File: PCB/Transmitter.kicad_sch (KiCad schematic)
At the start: 31 parts, among them T1 MABA-007159, U1 LTC5599IUF, U2 ADF4351

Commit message: new file:   Datasheet/HMC849A_RF_Switch_SPDT.pdf 	new file:   Datasheet/TG2016SMN_26MHz_MCGNNM_Oscillator.pdf 	modified:   PCB/DroidRadio.kicad_pro 	modified:   PCB/DroidRadio.kicad_sch 	modified:   PCB/Processors.kicad_sch 	modified:   PCB/Simulation/Transmitter_Side.pll 	modified:   PCB/Transmitter.kicad_sch 	deleted:    PCB/~DroidRadio.kicad_pro.lck
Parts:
- added C10, C23, C25: 10pF, symbol Device:C
- added C22, C24, C26, C28, C29, C30, C31, C32, C33, C34, C35, C9: 0.1uF, symbol Device:C
- added C27: 2.2nF, symbol Device:C
- added FL1: LFCN-1400, Filter:Filter_Mini-Circuits_FV1206, symbol RF_Filter:LFCN-1400
- added FL2: LFCN-2000, Filter:Filter_Mini-Circuits_FV1206, symbol RF_Filter:LFCN-2000
- added R7: 25.1k, symbol Device:R_US
- added R8: 23.1k, symbol Device:R_US
- added U3, U4: HMC849A, Package_DFN_QFN:QFN-24-1EP_4x4mm_P0.5mm_EP2.65x2.65mm_ThermalVias, symbol RF_Switch:HMC849A
- added Y1: TG2016SMN-26Mhz-MCGNNM, Crystal:Crystal_SMD_2016-4Pin_2.0x1.6mm, symbol Oscillator:TG2520SMN-xx.xxxxxxMhz-xxxxNM
- C17: value 2.7nF -> 3nF; Tolerance (none) -> 1%
- C18: value 220uF -> 30pF; Tolerance (none) -> 1%
- C19: value 0.1uF -> 39nF; Tolerance (none) -> 1%
- C20: value 1nF -> 1.2nF; Tolerance (none) -> 1%
- C21: value 330pF -> 180pF; Tolerance (none) -> 1%
- R2: value 5.1k, 1% -> 5.1k; Tolerance (none) -> 1%
- R3: value 220 -> 216; Tolerance (none) -> 1%
- R4: value 5 -> 19.1k
- R5: value 430 -> 442; Tolerance (none) -> 1%
- R6: value 30 -> 26.1k
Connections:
- net +3.3V: now also C9.2, Y1.4 (Vcc)
- net GND: now also C10.1, C22.1, C23.1, C24.1, C25.1, C26.1, C27.2, C28.1, C29.2, C9.1, FL1.2 (GND), FL1.4 (GND), FL2.2 (GND), FL2.4 (GND), U3.10 (GND), U3.11 (GND), U3.13 (GND), U3.14 (GND), U3.15 (GND), U3.16 (GND), U3.17 (GND), U3.4 (GND), U3.6 (GND), U3.7 (GND), U3.8 (GND), U4.10 (GND), U4.11 (GND), U4.13 (GND), U4.14 (GND), U4.15 (GND), U4.16 (GND), U4.17 (GND), U4.4 (GND), U4.6 (GND), U4.7 (GND), U4.8 (GND), Y1.2 (GND)
- net SPI_CLK: now also R7.2
- net at C1.1, L1.1: no longer T1.5
- net at C19.1: now also R3.2, C27.1; no longer R4.2
- net at C20.1, C21.1, U2.20 (VTUNE): now also R5.2; no longer R6.2
- net at C5.2, U1.19 (CSB): now also R8.1
- net at R6.1: now also C3.2, U1.21 (SDI); no longer R5.2
- net at C4.2, U1.20 (SCLK): now also R7.1
- net at R2.1: now also U2.22 (RSET); no longer U2.24 (VREF)
- net at R4.1: now also C2.2, R1.2, U1.22 (SDO); no longer R3.2
- net TXRF: now reaches U1.16 (RF)
- net SYN_RF_1P: now reaches U2.14 (RF_OUT_B+)
- net SYN_RF_1P: now also U2.15 (RF_OUT_B-)
- net at U2.19 (TEMP): now also C10.2, C22.2
- net at U2.23 (VCOM): now also C23.2, C24.2
- net SYN_LD: now reaches U2.25 (LD)
- net at U2.29 (REFIN): now also Y1.3 (OUT)
- net SYN_MUXOUT: now reaches U2.30 (MUXOUT)
- new net: C33.1, FL2.3 (OUT)
- new net: C33.2, U4.12 (RF2)
- new net: C31.1, U3.12 (RF2)
- new net: C31.2, FL2.1 (IN)
- new net: C35.1, U4.3 (RFC)
- new net: C29.1, U4.1 (VDD)
- new net: C32.2, U4.9 (RF1)
- new net: C34.1, T1.5
- new net: C34.2, U3.3 (RFC)
- new net: C30.1, U3.9 (RF1)
- new net: C30.2, FL1.1 (IN)
- new net: C28.2, U3.1 (VDD)
- new net: C25.2, C26.2, U2.24 (VREF)
- new net: C32.1, FL1.3 (OUT)
- new net IQM_CSB: R8.2
- new net IQM_SDI: R6.2
- new net IQM_SDO: R4.2
- new net LPFSW1_EN: U3.5 (EN)
- new net LPFSW1_VCTL: U3.2 (VCTL)
- no-connect marks 0 -> 1
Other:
- note added: "Product Number: X1G0054410304"
- note removed: "LPF needed?"
- moved on the sheet: C1, C11, C12, C13, C14, C15, C16, C17, C18, C2, C20, C21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

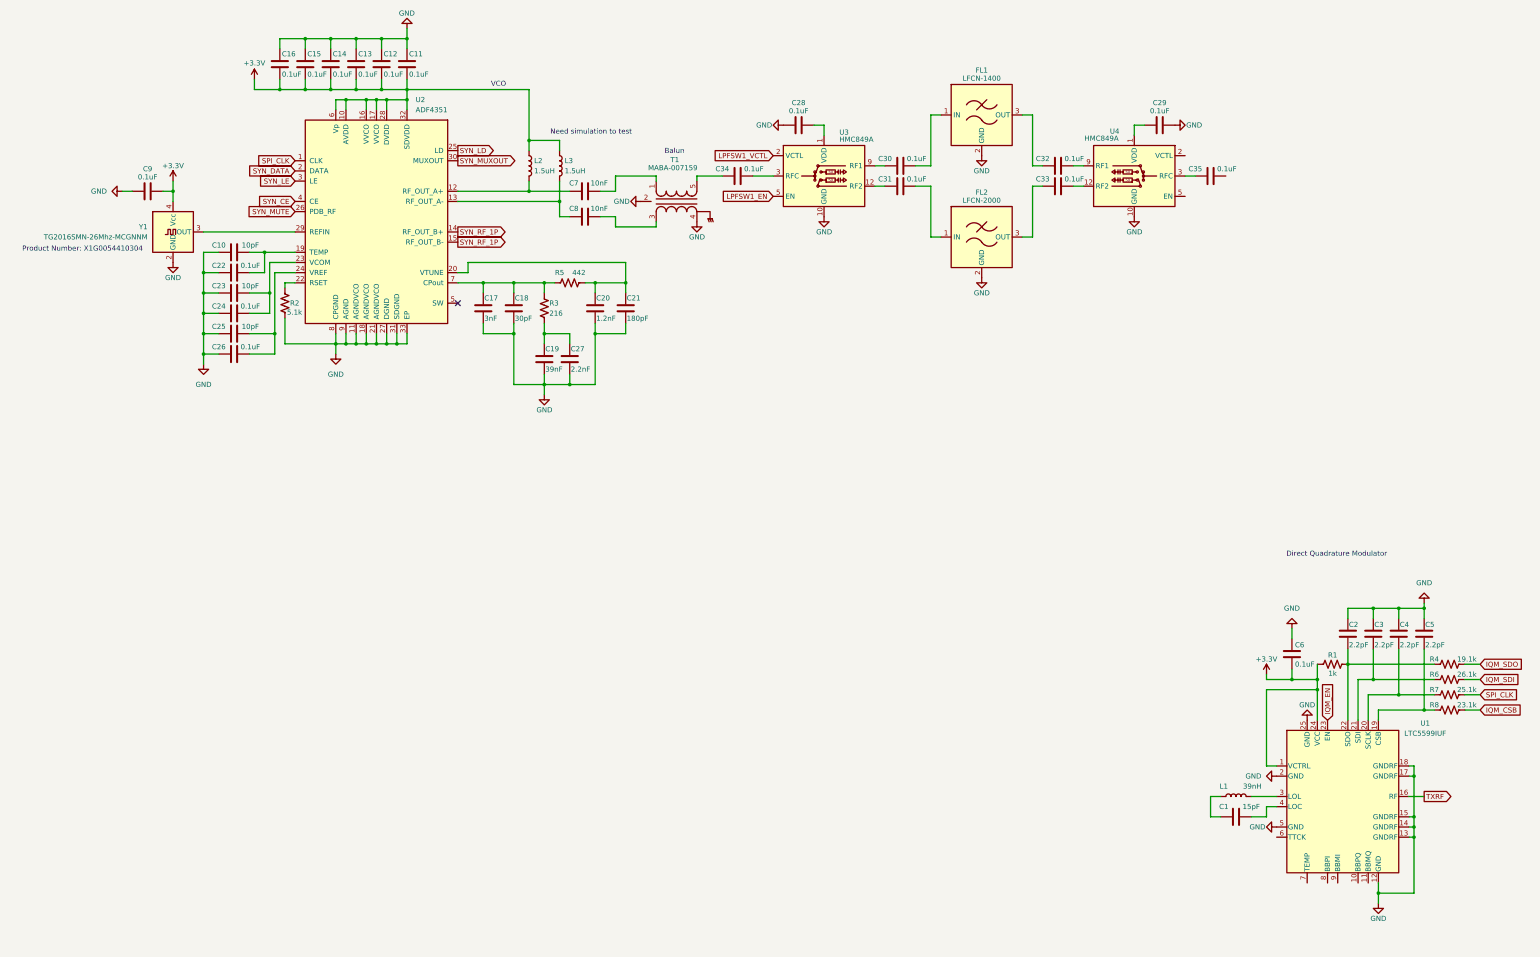
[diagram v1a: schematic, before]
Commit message: Add datasheets and update PCB schematics
Add LFCN-1400+ and LFCN-2000+ low-pass filter datasheets, plus STM32H43VI MCU and TMP411 temperature sensor datasheets. Update DroidRadio.kicad_pro, Processors.kicad_sch and Transmitter.kicad_sch.
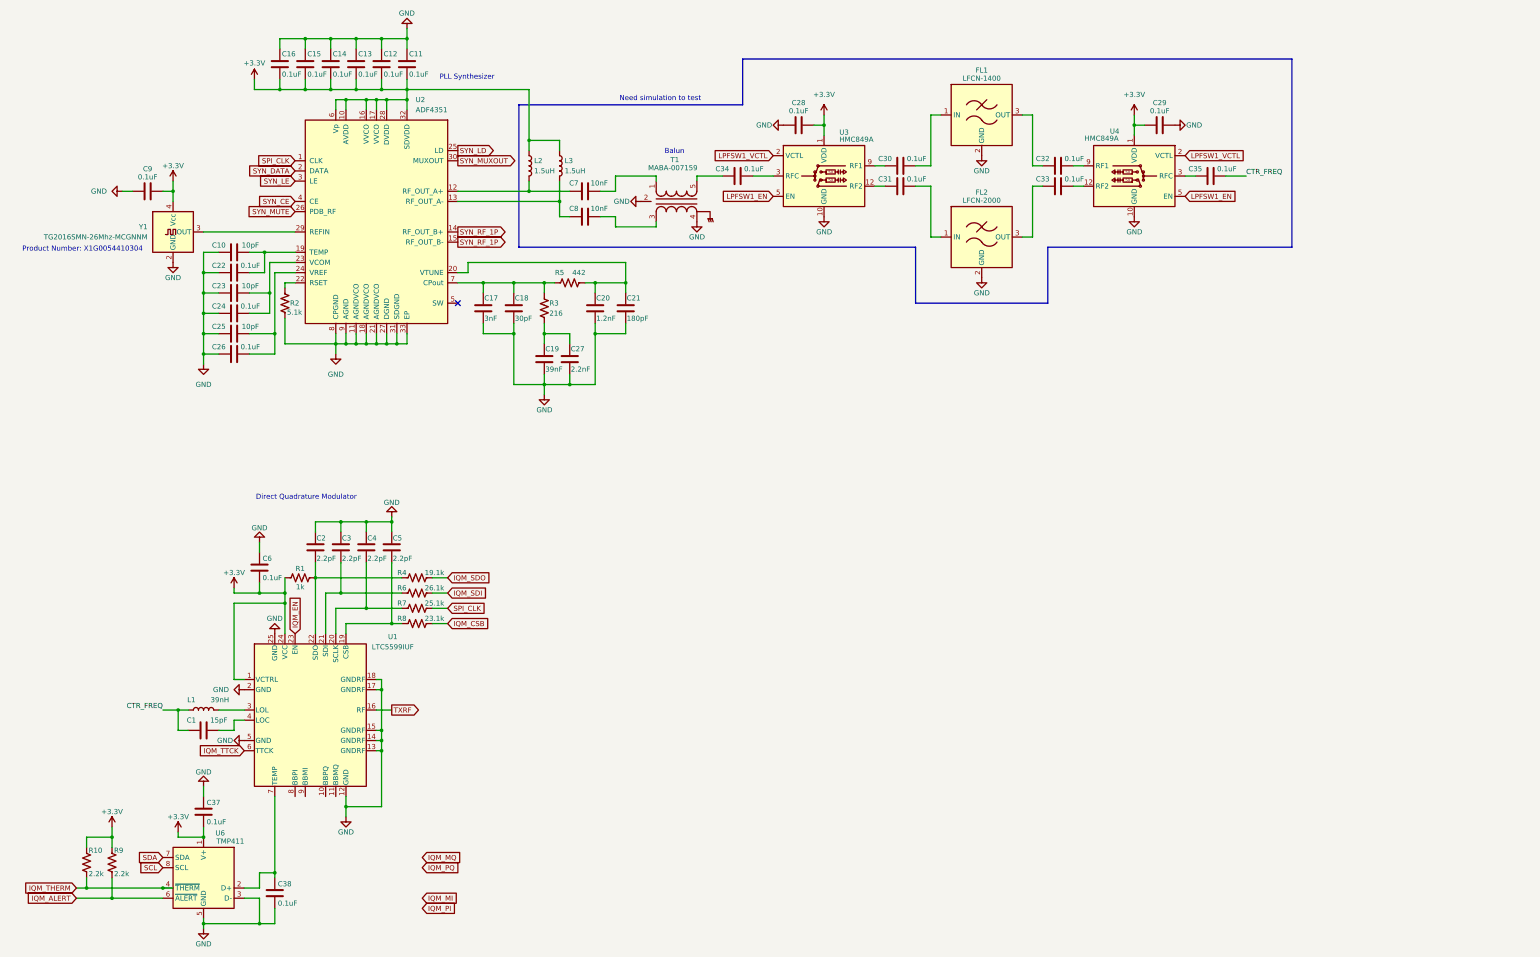
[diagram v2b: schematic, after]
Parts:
- added C37, C38: 0.1uF, symbol Device:C
- added R10, R9: 2.2k, symbol Device:R_US
- added U6: TMP411, symbol Sensor_Temperature:TMP411
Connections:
- net +3.3V: now also C28.2, C29.1, U3.1 (VDD), U4.1 (VDD), C37.2, R10.1, R9.1, U6.1 (V+)
- net GND: now also C37.1, C38.2, U6.3 (D-), U6.5 (GND)
- net LPFSW1_EN: now also U4.5 (EN)
- net LPFSW1_VCTL: now also U4.2 (VCTL)
- net CTR_FREQ: now reaches C35.2
- net CTR_FREQ: now also C1.1, L1.1
- net IQM_TTCK: now reaches U1.6 (TTCK)
- net at U1.7 (TEMP): now also C38.1, U6.2 (D+)
- new net IQM_ALERT: R9.2, U6.6 (~{ALERT})
- new net IQM_THERM: R10.2, U6.4 (~{THERM})
- new net SCL: U6.8 (SCL)
- new net SDA: U6.7 (SDA)
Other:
- note added: "PLL Synthesizer"
- note removed: "VCO"
- moved on the sheet: C1, C2, C3, C4, C5, C6, L1, R1, R4, R6, R7, R8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

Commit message: Updated PCB schematics, added new datasheet and components library
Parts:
- added U7: DAC5652IPFB, Package_QFP:TQFP-48_7x7mm_P0.5mm, symbol DroidRadio:DAC5652IPFB
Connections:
- net SYN_RF_1P: no longer U2.15 (RF_OUT_B-)
- new net SYN_RF_1N: U2.15 (RF_OUT_B-)
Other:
- note added: "A Frequency divider needed here."
- moved on the sheet: C1, C10, C11, C12, C13, C14, C15, C16, C17, C18, C19, C2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
